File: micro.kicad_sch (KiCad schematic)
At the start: 7 parts, among them SW2 SW_MEC_5G_LED

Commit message: updated MCU COMMS
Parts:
- C10: value 10uf -> 1uf
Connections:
- net ~{RST}: now reaches C10.1, R10.2, R9.1, SW2.4 (A), U1.24 (~{RST})
- net UART_RX: now reaches U1.3 (P1.1/CA1)
- net UART_TX: now reaches U1.4 (P1.2/CA2)
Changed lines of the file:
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@@
+		)
+	)
+	(text_box "Need to add XTAL OSC"
+		(exclude_from_sim no)
+		(at 176.53 20.32 0)
+		(size 29.21 16.51)
+		(margins 0.9525 0.9525 0.9525 0.9525)
+		(stroke
+			(width 0)
+			(type solid)
+		)
+		(fill
+			(type none)
+		)
+		(effects
+			(font
+				(size 1.27 1.27)
+			)
+			(justify left top)
 		)
 	)
@@
 	)
 	(junction
+		(at 219.71 67.31)
+		(diameter 0)
+		(color 0 0 0 0)
+	)
+	(junction
 		(at 233.68 67.31)
 		(diameter 0)
@@
 	(wire
 		(pts
+			(xy 142.24 62.23) (xy 146.05 62.23)
+		)
+		(stroke
+			(width 0)
+			(type default)
+		)
+	)
+	(wire
+		(pts
 			(xy 243.84 67.31) (xy 243.84 66.04)
 		)
@@
 	(wire
 		(pts
+			(xy 219.71 62.23) (xy 219.71 67.31)
+		)
+		(stroke
+			(width 0)
+			(type default)
+		)
+	)
+	(wire
+		(pts
 			(xy 193.04 62.23) (xy 199.39 62.23)
 		)
@@
 	(wire
 		(pts
+			(xy 219.71 67.31) (xy 231.14 67.31)
+		)
+		(stroke
+			(width 0)
+			(type default)
+		)
+	)
+	(wire
+		(pts
 			(xy 233.68 93.98) (xy 231.14 93.98)
 		)
@@
 	(wire
 		(pts
+			(xy 142.24 64.77) (xy 146.05 64.77)
+		)
+		(stroke
+			(width 0)
+			(type default)
+		)
+	)
+	(wire
+		(pts
 			(xy 231.14 67.31) (xy 233.68 67.31)
 		)
@@
 	(wire
 		(pts
-			(xy 215.9 67.31) (xy 231.14 67.31)
+			(xy 215.9 67.31) (xy 219.71 67.31)
 		)
 		(stroke
@@
 			(width 0)
 			(type default)
+		)
+	)
+	(global_label "UART_TX"
+		(shape output)
+		(at 142.24 64.77 180)
+		(fields_autoplaced yes)
+		(effects
+			(font
+				(size 0.889 0.889)
+			)
+			(justify right)
+		)
+		(property "Intersheetrefs" "${INTERSHEET_REFS}"
+			(at 134.6896 64.77 0)
+			(effects
+				(font
+					(size 1.27 1.27)
+				)
+				(justify right)
+				(hide yes)
+			)
 		)
 	)
@@
 		)
 	)
+	(global_label "~{RST}"
+		(shape output)
+		(at 219.71 62.23 90)
+		(fields_autoplaced yes)
+		(effects
+			(font
+				(size 0.889 0.889)
+			)
+			(justify left)
+		)
+		(property "Intersheetrefs" "${INTERSHEET_REFS}"
+			(at 219.71 57.7275 90)
+			(effects
+				(font
+					(size 1.27 1.27)
+				)
+				(justify left)
+				(hide yes)
+			)
+		)
+	)
 	(global_label "UNUSED_6"
 		(shape output)
@@
 		(property "Intersheetrefs" "${INTERSHEET_REFS}"
 			(at 133.2926 77.47 0)
+			(effects
+				(font
+					(size 1.27 1.27)
+				)
+				(justify right)
+				(hide yes)
+			)
+		)
+	)
+	(global_label "UART_RX"
+		(shape input)
+		(at 142.24 62.23 180)
+		(fields_autoplaced yes)
+		(effects
+			(font
+				(size 0.889 0.889)
+			)
+			(justify right)
+		)
+		(property "Intersheetrefs" "${INTERSHEET_REFS}"
+			(at 134.4779 62.23 0)
 			(effects
 				(font
@@
 			)
 		)
-		(property "Value" "10uf"
+		(property "Value" "1uf"
 			(at 219.202 78.994 0)
 			(effects

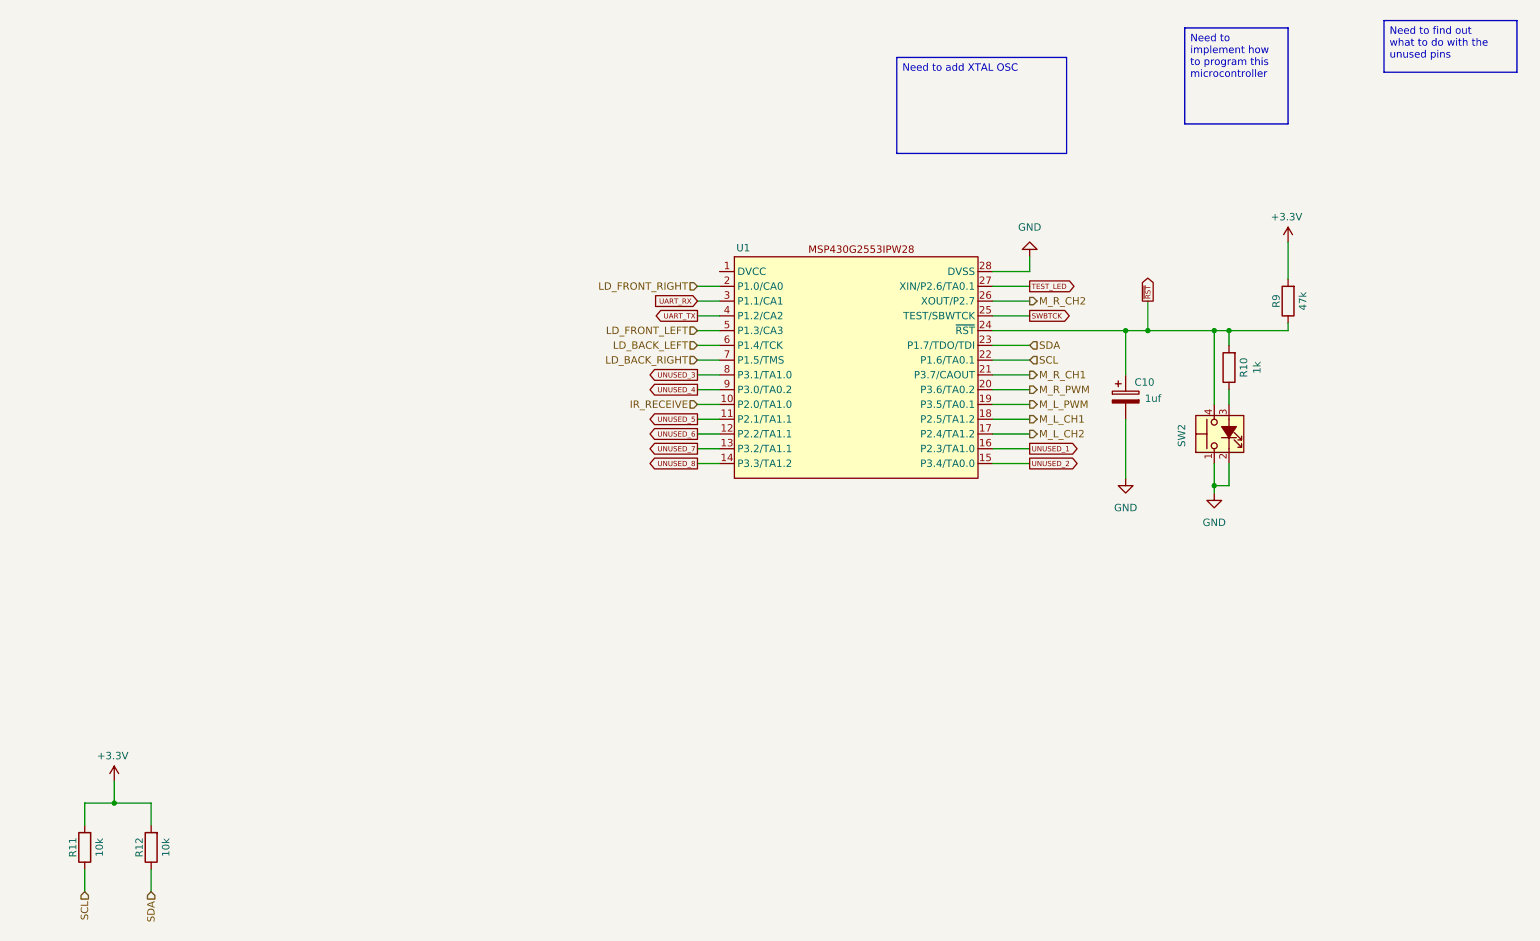
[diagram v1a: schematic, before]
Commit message: updated MCU schematic
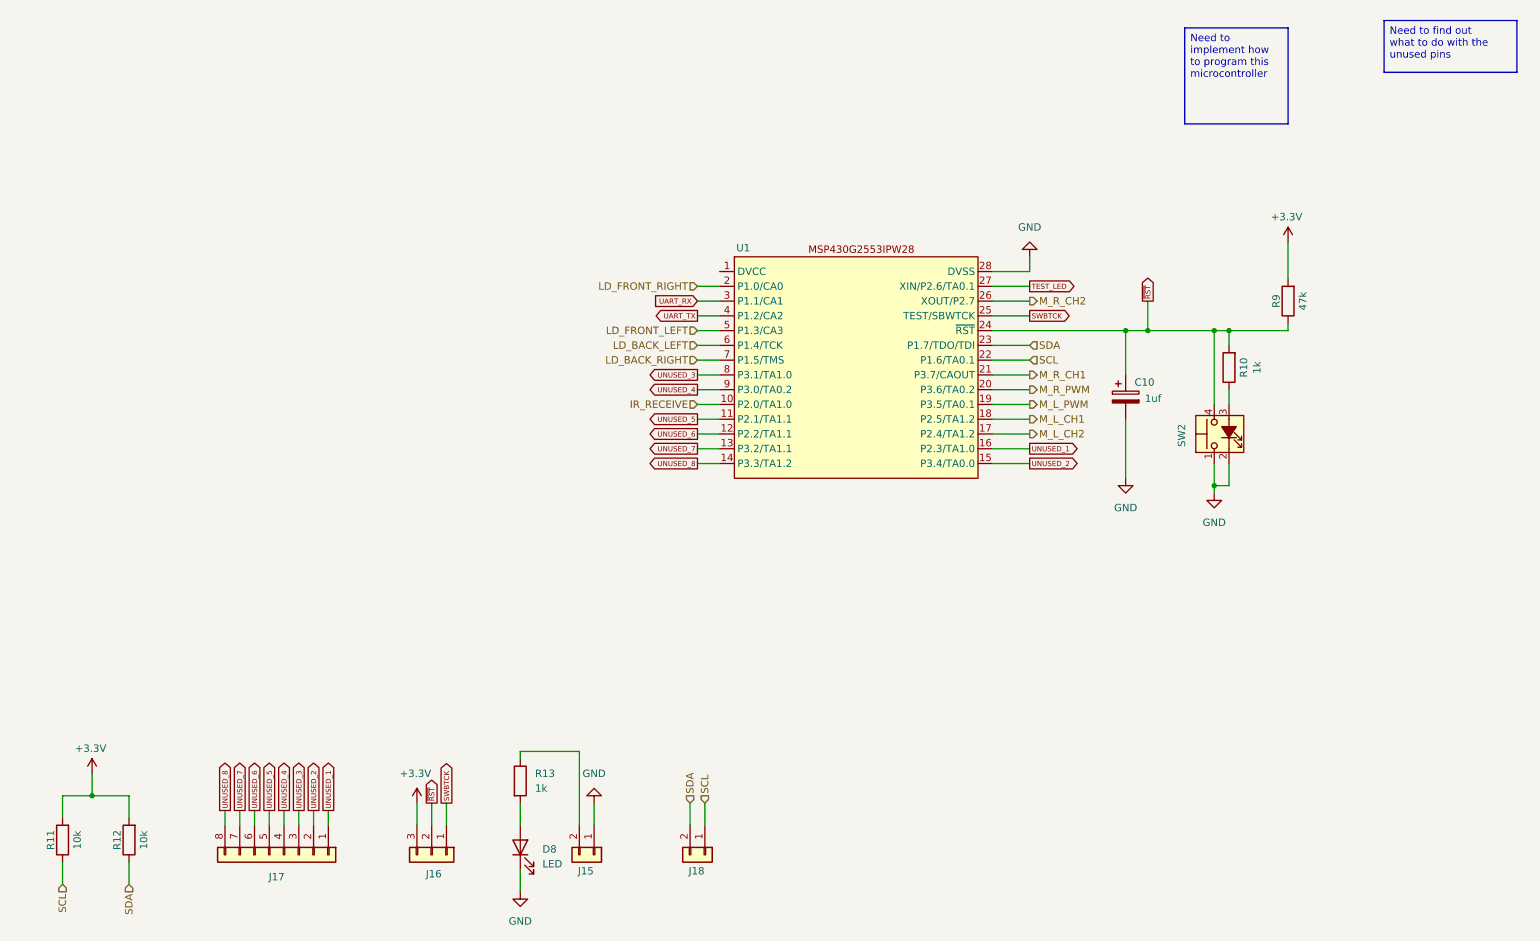
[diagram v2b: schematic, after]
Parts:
- added D8: LED, LED_SMD:LED_1210_3225Metric, symbol Device:LED
- added J15, J18: Conn_01x02, symbol Connector_Generic:Conn_01x02
- added J16: Conn_01x03, symbol Connector_Generic:Conn_01x03
- added J17: Conn_01x08, symbol Connector_Generic:Conn_01x08
- added R13: 1k, Resistor_SMD:R_1210_3225Metric, symbol Device:R
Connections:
- net +3.3V: now also J16.3 (Pin_3)
- net GND: now also D8.1 (K), J15.1 (Pin_1)
- net SCL: now also J18.1 (Pin_1)
- net SDA: now also J18.2 (Pin_2)
- net SWBTCK: now also J16.1 (Pin_1)
- net UNUSED_1: now also J17.1 (Pin_1)
- net UNUSED_2: now also J17.2 (Pin_2)
- net UNUSED_3: now also J17.3 (Pin_3)
- net UNUSED_4: now also J17.4 (Pin_4)
- net UNUSED_5: now also J17.5 (Pin_5)
- net UNUSED_6: now also J17.6 (Pin_6)
- net UNUSED_7: now also J17.7 (Pin_7)
- net UNUSED_8: now also J17.8 (Pin_8)
- net ~{RST}: now also J16.2 (Pin_2)
- new net: D8.2 (A), R13.2
- new net: J15.2 (Pin_2), R13.1
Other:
- moved on the sheet: R11, R12

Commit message: removed mechanical sheet
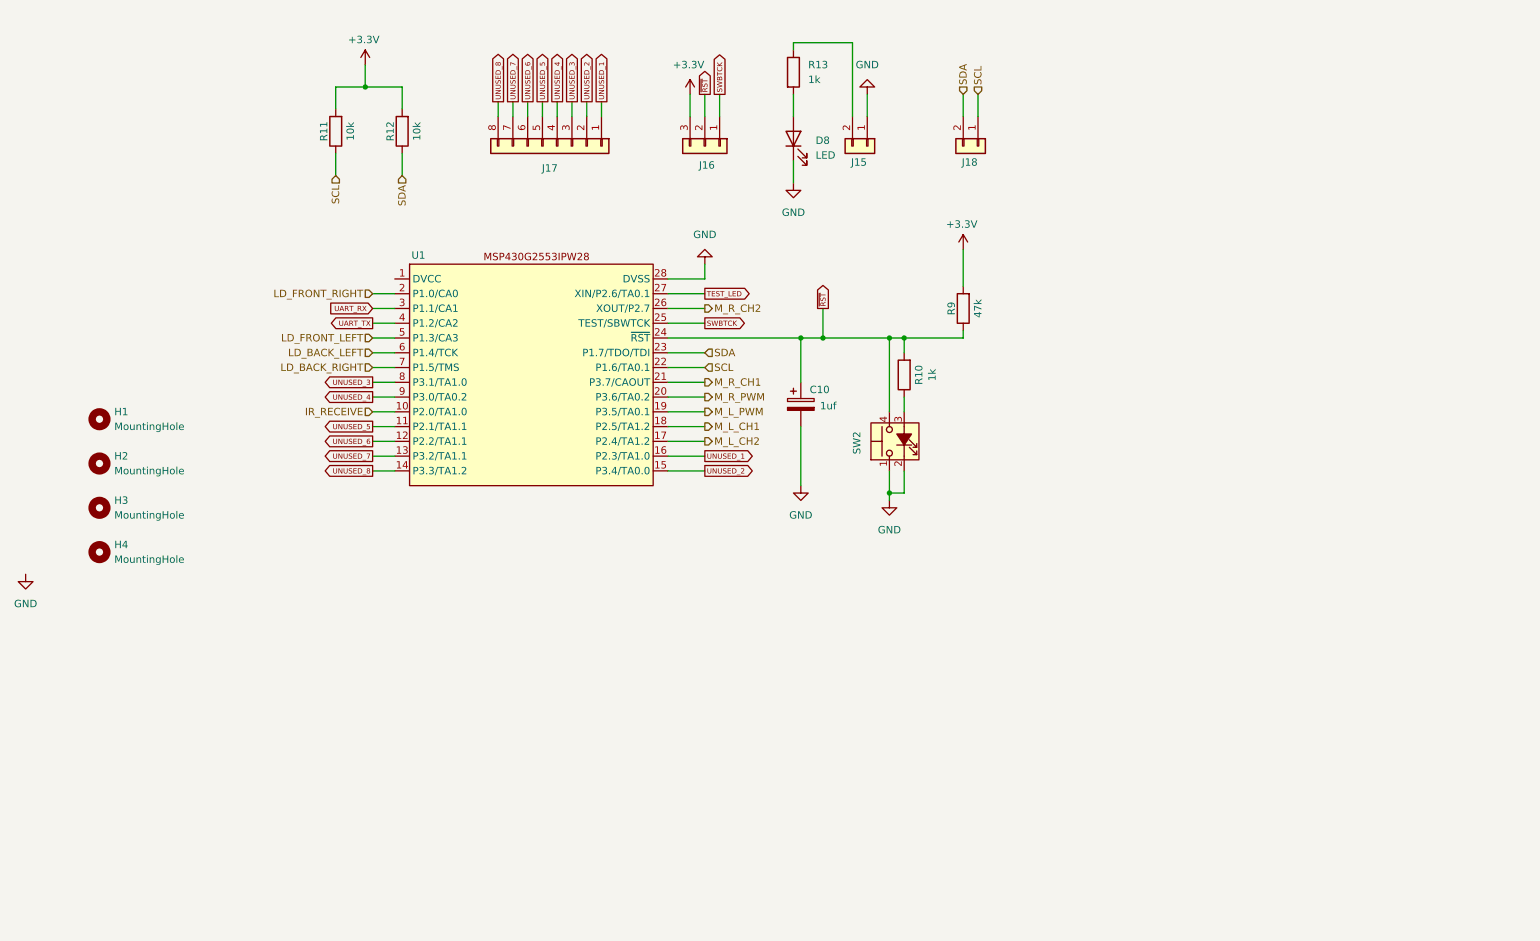
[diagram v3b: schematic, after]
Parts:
- added H1, H2, H3, H4: MountingHole, MountingHole:MountingHole_6.4mm_M6, symbol Mechanical:MountingHole
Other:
- moved on the sheet: C10, D8, J15, J16, J17, J18, R10, R11, R12, R13, R9, SW2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

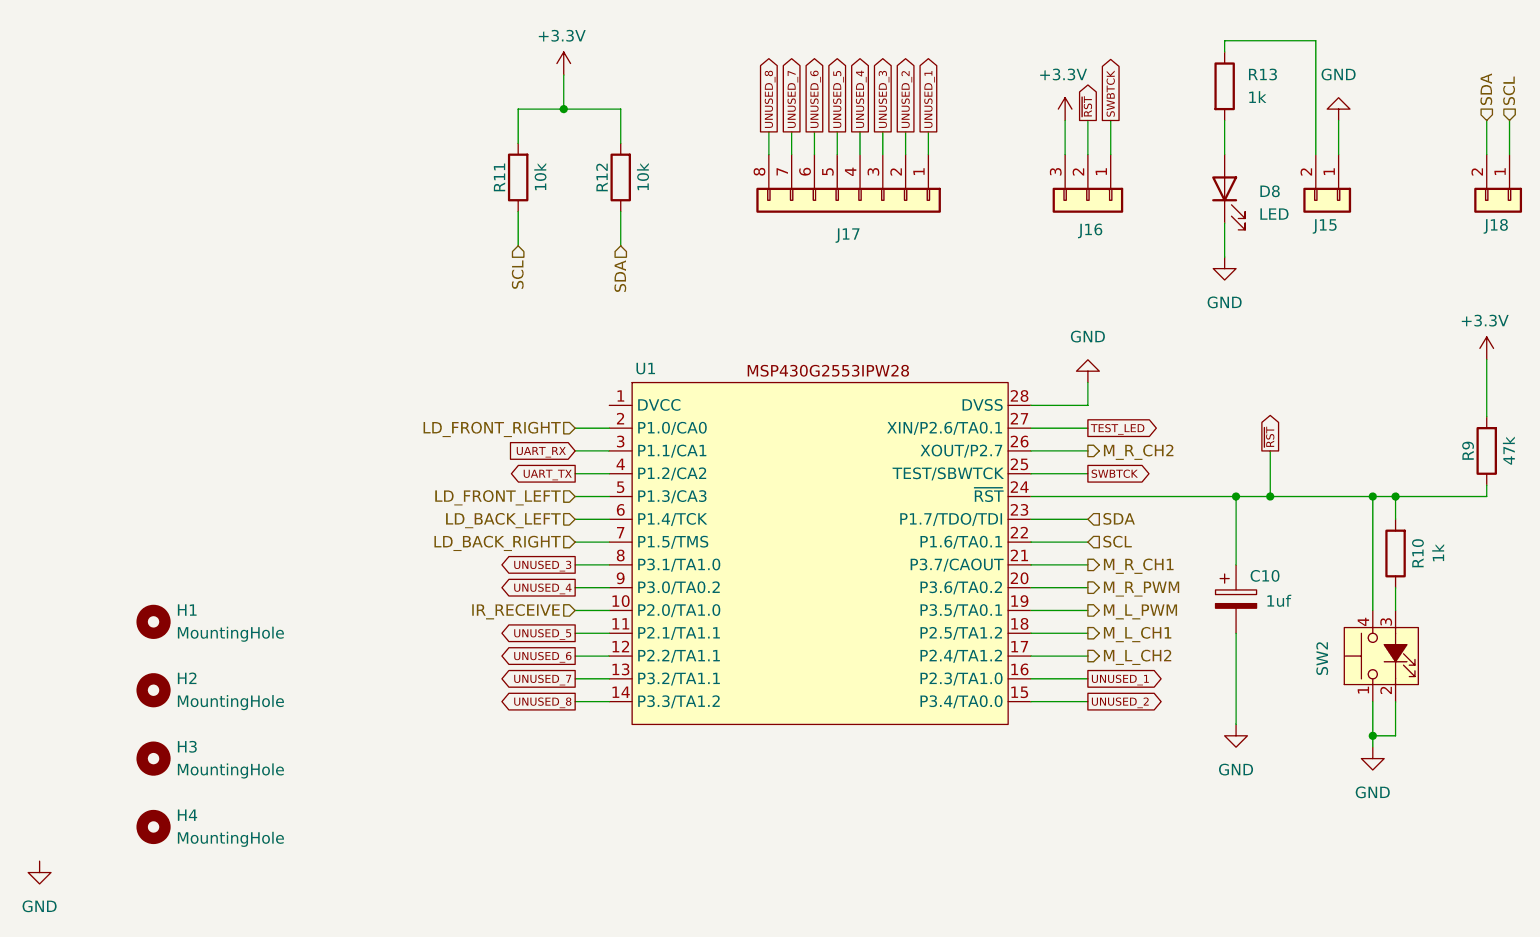
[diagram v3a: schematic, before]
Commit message: finalized schematic
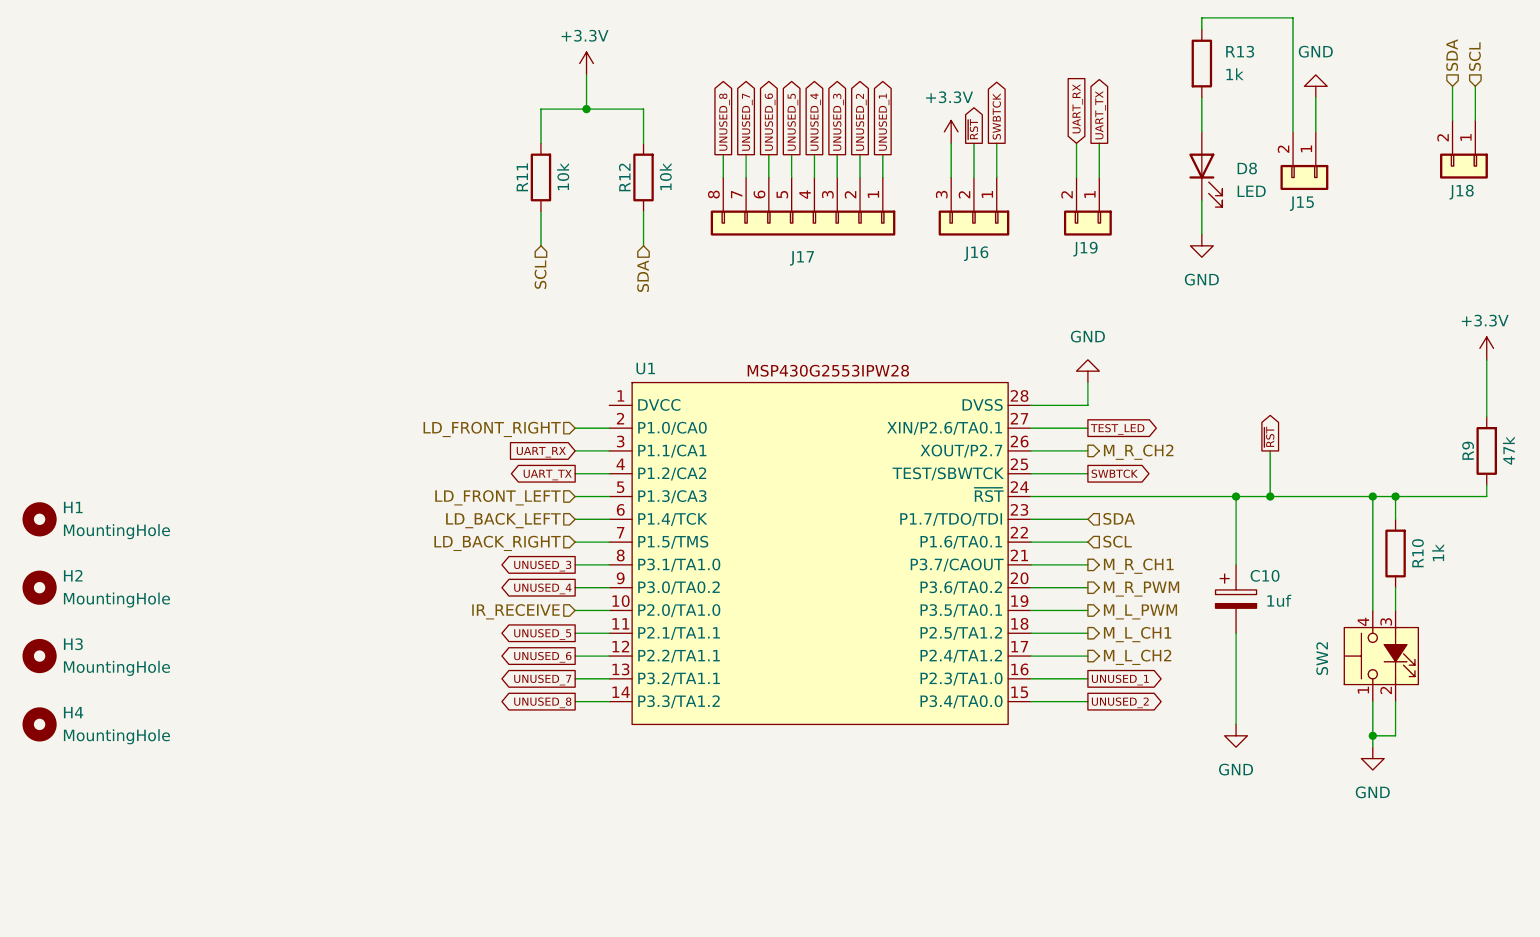
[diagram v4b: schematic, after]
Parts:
- added J19: Conn_01x02, symbol Connector_Generic:Conn_01x02
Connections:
- net UART_RX: now also J19.2 (Pin_2)
- net UART_TX: now also J19.1 (Pin_1)
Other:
- moved on the sheet: D8, H1, H2, H3, H4, J15, J16, J17, J18, R11, R12, R13
